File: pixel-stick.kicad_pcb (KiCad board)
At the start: 2 copper layers, 16.5 x 37.1 mm, 16 parts, among them J2 WS28**, U1 AZ1117-3.3, U2 ESP-01v090, U3 SN74LVC1T45DBV, U4 RT9361A

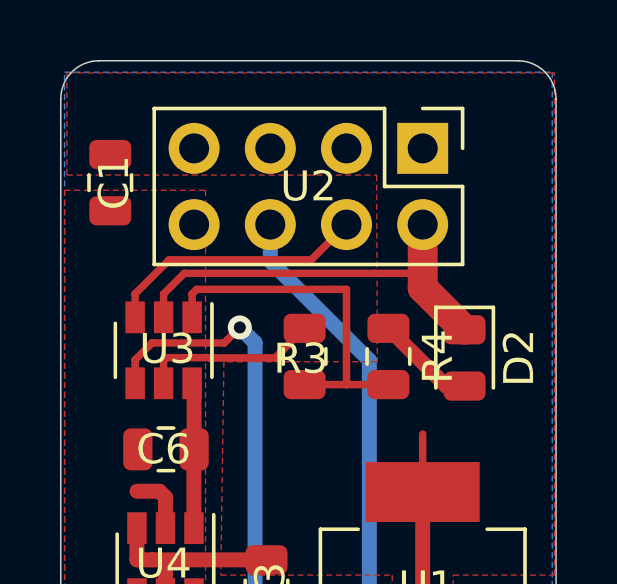
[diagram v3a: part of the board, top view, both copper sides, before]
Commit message: remove programming features
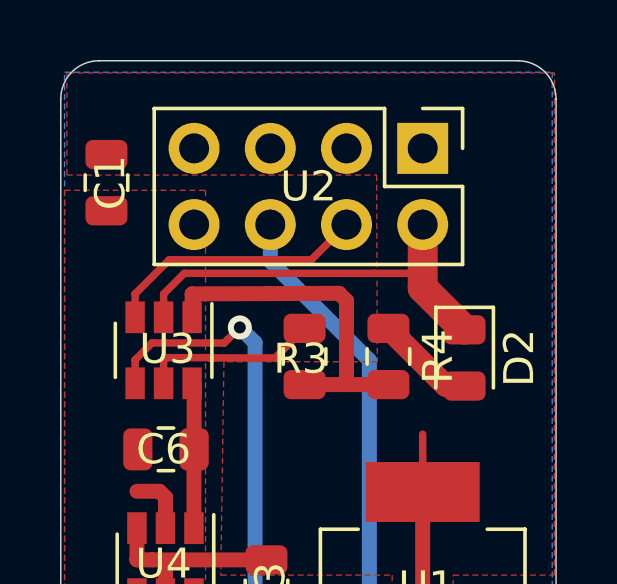
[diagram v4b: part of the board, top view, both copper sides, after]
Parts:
- moved C1 0.13 mm to (44.1, 57.7)
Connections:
- U2 pad 5: /~RST -> +3V3
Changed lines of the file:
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@@
     (thickness 1.6)
     (drawings 13)
-    (tracks 58)
+    (tracks 57)
     (zones 0)
     (modules 16)
-    (nets 17)
+    (nets 16)
   )
   (page A4)
@@
   )
   (setup
-    (last_trace_width 1)
+    (last_trace_width 0.25)
     (user_trace_width 0.5)
     (user_trace_width 1)
@@
   (net 11 /DATA)
   (net 12 /GPIO0)
-  (net 13 /~RST)
-  (net 14 /GPIO2)
-  (net 15 "Net-(R3-Pad1)")
-  (net 16 "Net-(D2-Pad2)")
+  (net 13 /GPIO2)
+  (net 14 "Net-(R3-Pad1)")
+  (net 15 "Net-(D2-Pad2)")
   (net_class Default "This is the default net class."
     (clearance 0.2)
@@
     (add_net /TXD)
     (add_net /VIN)
-    (add_net /~RST)
     (add_net GND)
     (add_net "Net-(C5-Pad1)")
@@
     (fp_line (start 1 -0.6) (end -0.7 -0.6) (layer F.Fab) (width 0.1))
     (pad 2 smd roundrect (at 0.9375 0 270) (size 0.975 1.4) (layers F.Cu F.Paste F.Mask) (roundrect_rratio 0.25)
-      (net 16 "Net-(D2-Pad2)"))
+      (net 15 "Net-(D2-Pad2)"))
     (pad 1 smd roundrect (at -0.9375 0 270) (size 0.975 1.4) (layers F.Cu F.Paste F.Mask) (roundrect_rratio 0.25)
       (net 1 GND))
@@
       (net 2 +3V3))
     (pad 1 smd roundrect (at -0.9375 0 270) (size 0.975 1.4) (layers F.Cu F.Paste F.Mask) (roundrect_rratio 0.25)
-      (net 16 "Net-(D2-Pad2)"))
+      (net 15 "Net-(D2-Pad2)"))
     (model ${KISYS3DMOD}/Resistor_SMD.3dshapes/R_0805_2012Metric.wrl
       (at (xyz 0 0 0))
@@
       (net 12 /GPIO0))
     (pad 5 thru_hole oval (at 0 5.08 270) (size 1.7 1.7) (drill 1) (layers *.Cu *.Mask)
-      (net 13 /~RST))
+      (net 2 +3V3))
     (pad 4 thru_hole oval (at 2.54 2.54 270) (size 1.7 1.7) (drill 1) (layers *.Cu *.Mask)
-      (net 14 /GPIO2))
+      (net 13 /GPIO2))
     (pad 3 thru_hole oval (at 0 2.54 270) (size 1.7 1.7) (drill 1) (layers *.Cu *.Mask)
       (net 2 +3V3))
@@
     )
     (pad 5 smd rect (at 1.1 0 270) (size 1.06 0.65) (layers F.Cu F.Paste F.Mask)
-      (net 15 "Net-(R3-Pad1)"))
+      (net 14 "Net-(R3-Pad1)"))
     (pad 6 smd rect (at 1.1 -0.95 270) (size 1.06 0.65) (layers F.Cu F.Paste F.Mask)
       (net 6 +5V))
@@
       (net 11 /DATA))
     (pad 3 smd rect (at -1.1 0.95 270) (size 1.06 0.65) (layers F.Cu F.Paste F.Mask)
-      (net 14 /GPIO2))
+      (net 13 /GPIO2))
     (pad 2 smd rect (at -1.1 0 270) (size 1.06 0.65) (layers F.Cu F.Paste F.Mask)
       (net 1 GND))
@@
       (net 2 +3V3))
     (pad 1 smd roundrect (at -0.9375 0 270) (size 0.975 1.4) (layers F.Cu F.Paste F.Mask) (roundrect_rratio 0.25)
-      (net 15 "Net-(R3-Pad1)"))
+      (net 14 "Net-(R3-Pad1)"))
     (model ${KISYS3DMOD}/Resistor_SMD.3dshapes/R_0805_2012Metric.wrl
       (at (xyz 0 0 0))
@@
   )
   (module Capacitor_SMD:C_0805_2012Metric (layer F.Cu)
-    (at 44.196 57.658 270)
+    (at 44.069 57.658 270)
     (descr "Capacitor SMD 0805 (2012 Metric), square (rectangular) end terminal, IPC_7351 nominal, (Body size source: https://docs.google.com/spreadsheets/d/1BsfQQcO9C6DZCsRaXUlFlo91Tg2WpOkGARC1WS5S8t0/edit?usp=sharing), generated with kicad-footprint-generator")
     (tags capacitor)
@@
   (segment (start 52.04 56.485) (end 52.07 56.515) (width 0.25) (layer B.Cu) (net 2))
   (segment (start 54.61 74.27) (end 54.61 67.97) (width 0.5) (layer F.Cu) (net 2))
-  (segment (start 46.924 61.366) (end 47.076 61.214) (width 0.25) (layer F.Cu) (net 2))
-  (segment (start 46.924 62.146) (end 46.924 61.366) (width 0.25) (layer F.Cu) (net 2))
   (segment (start 54.61 66.04) (end 54.61 67.97) (width 0.25) (layer F.Cu) (net 2))
   (segment (start 45.085 69.174) (end 45.085 70.231) (width 0.5) (layer F.Cu) (net 2))
@@
   (segment (start 45.593 70.231) (end 49.403 70.231) (width 0.5) (layer F.Cu) (net 2))
   (segment (start 45.085 70.231) (end 45.593 70.231) (width 0.5) (layer F.Cu) (net 2))
-  (segment (start 47.076 61.214) (end 51.532 61.214) (width 0.25) (layer F.Cu) (net 2))
-  (segment (start 52.07 64.389) (end 52.07 61.214) (width 0.25) (layer F.Cu) (net 2))
-  (segment (start 51.532 61.214) (end 52.07 61.214) (width 0.25) (layer F.Cu) (net 2))
-  (segment (start 50.673 64.389) (end 52.07 64.389) (width 0.25) (layer F.Cu) (net 2))
-  (segment (start 52.07 64.389) (end 53.467 64.389) (width 0.25) (layer F.Cu) (net 2))
+  (segment (start 50.673 64.389) (end 52.07 64.389) (width 0.5) (layer F.Cu) (net 2))
+  (segment (start 52.07 64.389) (end 53.467 64.389) (width 0.5) (layer F.Cu) (net 2))
+  (segment (start 46.924 62.146) (end 46.924 61.366) (width 0.5) (layer F.Cu) (net 2))
+  (segment (start 52.07 61.595) (end 51.820716 61.345716) (width 0.5) (layer F.Cu) (net 2))
+  (segment (start 52.07 64.389) (end 52.07 61.595) (width 0.5) (layer F.Cu) (net 2))
+  (segment (start 46.924 61.366) (end 51.820716 61.345716) (width 0.5) (layer F.Cu) (net 2))
   (segment (start 45.115 71.404) (end 45.085 71.374) (width 0.5) (layer F.Cu) (net 4))
   (segment (start 45.115 73.914) (end 45.115 71.404) (width 0.5) (layer F.Cu) (net 4))
@@
   (segment (start 49.53 60.276314) (end 52.832 63.578314) (width 0.5) (layer B.Cu) (net 12))
   (segment (start 49.53 59.055) (end 49.53 60.276314) (width 0.5) (layer B.Cu) (net 12))
-  (segment (start 45.024 61.366) (end 45.024 62.146) (width 0.25) (layer F.Cu) (net 14))
-  (segment (start 46.159999 60.230001) (end 45.024 61.366) (width 0.25) (layer F.Cu) (net 14))
-  (segment (start 50.894999 60.230001) (end 46.159999 60.230001) (width 0.25) (layer F.Cu) (net 14))
-  (segment (start 52.07 59.055) (end 50.894999 60.230001) (width 0.25) (layer F.Cu) (net 14))
-  (segment (start 49.687 63.5) (end 50.673 62.514) (width 0.25) (layer F.Cu) (net 15))
-  (segment (start 46.049001 63.490999) (end 47.509001 63.490999) (width 0.25) (layer F.Cu) (net 15))
-  (segment (start 47.518002 63.5) (end 49.687 63.5) (width 0.25) (layer F.Cu) (net 15))
-  (segment (start 47.509001 63.490999) (end 47.518002 63.5) (width 0.25) (layer F.Cu) (net 15))
-  (segment (start 45.974 63.566) (end 46.049001 63.490999) (width 0.25) (layer F.Cu) (net 15))
-  (segment (start 45.974 64.346) (end 45.974 63.566) (width 0.25) (layer F.Cu) (net 15))
-  (segment (start 55.369 64.389) (end 55.372 64.392) (width 0.25) (layer F.Cu) (net 16))
-  (segment (start 55.3905 64.4375) (end 56.007 64.4375) (width 0.5) (layer F.Cu) (net 16))
-  (segment (start 53.467 62.514) (end 55.3905 64.4375) (width 0.5) (layer F.Cu) (net 16))
+  (segment (start 45.024 61.366) (end 45.024 62.146) (width 0.25) (layer F.Cu) (net 13))
+  (segment (start 50.894999 60.230001) (end 46.159999 60.230001) (width 0.25) (layer F.Cu) (net 13))
+  (segment (start 52.07 59.055) (end 50.894999 60.230001) (width 0.25) (layer F.Cu) (net 13))
+  (segment (start 46.159999 60.230001) (end 45.024 61.366) (width 0.25) (layer F.Cu) (net 13))
+  (segment (start 49.687 63.5) (end 50.673 62.514) (width 0.25) (layer F.Cu) (net 14))
+  (segment (start 46.049001 63.490999) (end 47.509001 63.490999) (width 0.25) (layer F.Cu) (net 14))
+  (segment (start 47.518002 63.5) (end 49.687 63.5) (width 0.25) (layer F.Cu) (net 14))
+  (segment (start 47.509001 63.490999) (end 47.518002 63.5) (width 0.25) (layer F.Cu) (net 14))
+  (segment (start 45.974 63.566) (end 46.049001 63.490999) (width 0.25) (layer F.Cu) (net 14))
+  (segment (start 45.974 64.346) (end 45.974 63.566) (width 0.25) (layer F.Cu) (net 14))
+  (segment (start 55.369 64.389) (end 55.372 64.392) (width 0.25) (layer F.Cu) (net 15))
+  (segment (start 55.3905 64.4375) (end 56.007 64.4375) (width 0.5) (layer F.Cu) (net 15))
+  (segment (start 53.467 62.514) (end 55.3905 64.4375) (width 0.75) (layer F.Cu) (net 15))
   (zone (net 1) (net_name GND) (layer F.Cu) (hatch edge 0.508)
     (connect_pads (clearance 0.508))

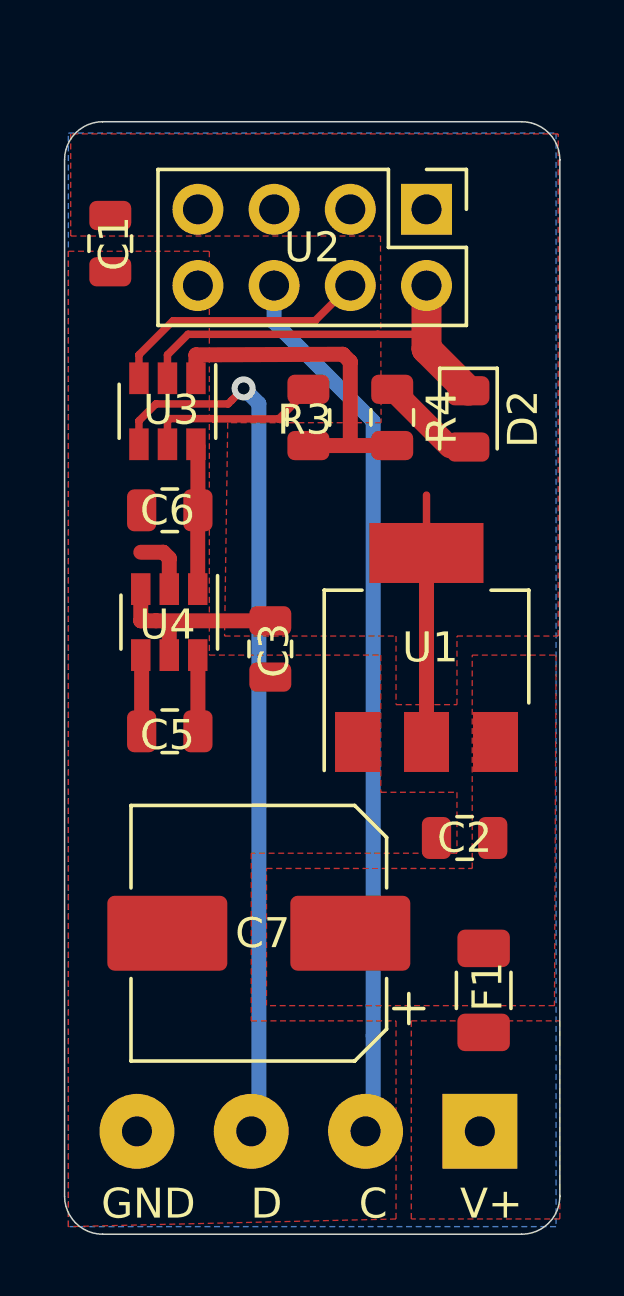
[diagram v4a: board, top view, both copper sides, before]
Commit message: cleanup silkscreen layer
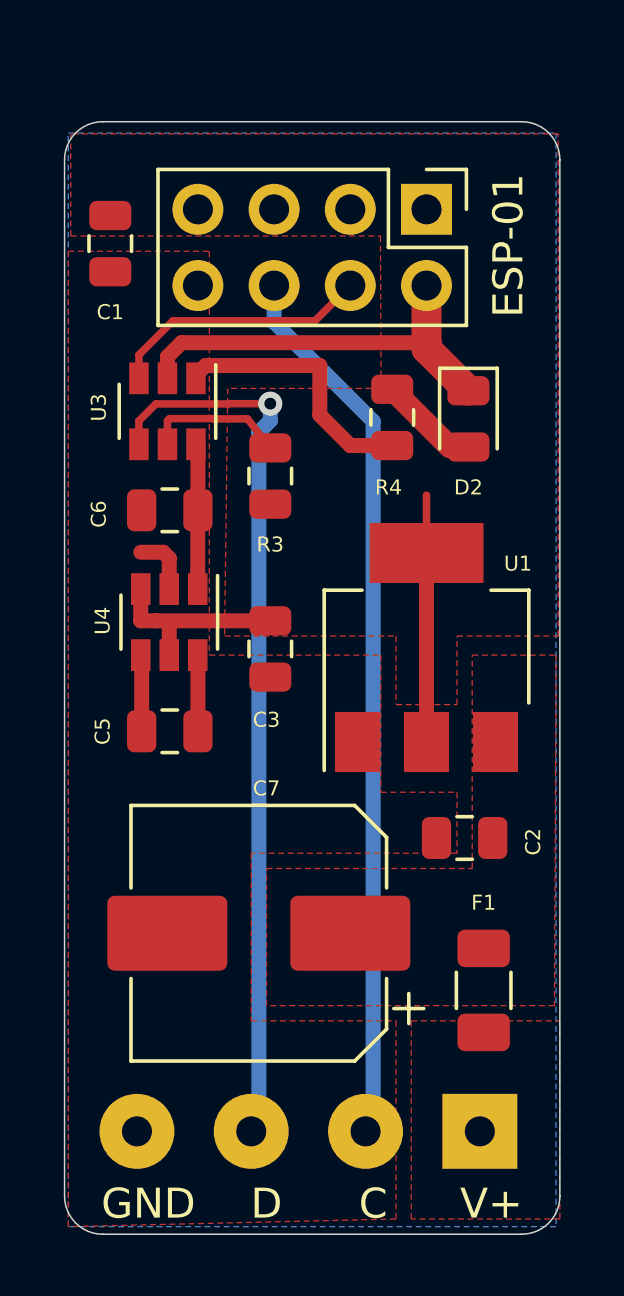
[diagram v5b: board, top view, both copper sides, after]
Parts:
- moved R3 2.33 mm to (49.4, 65.4)
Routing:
- net +3V3: track 26.3 -> 23.6 mm
- net Net-(R3-Pad1): track 5.92 -> 5.09 mm
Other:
- board text added: "ESP-01"

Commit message: update silkscreen
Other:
- board text added: "Board Version: 20191206a"
- board text added: "Designed by Kyle Klaus and Scotty Neally in CA"
- board text added: "This is a modified version of the ESPixelStick hardware design by Shelby Merrick. This board is designed to accept a pre-programmed ESP-01 module with the ESPixelStick firmware and operate 5V or 12V WS28xx pixel strings. The board is powered by the bus voltage of the light string and handles all voltage regulation. A 1A poly fuse is included to reduce the risk of damaging the board but no other p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"
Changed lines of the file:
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@@
   (general
     (thickness 1.6)
-    (drawings 14)
+    (drawings 17)
     (tracks 60)
     (zones 0)
@@
   )
   (setup
-    (last_trace_width 0.5)
+    (last_trace_width 0.25)
     (user_trace_width 0.5)
     (user_trace_width 1)
@@
     )
   )
+  (gr_text "Board Version: 20191206a" (at 54.9275 73.151999 90) (layer B.SilkS)
+    (effects (font (size 0.5 0.5) (thickness 0.125)) (justify mirror))
+  )
+  (gr_text "This is a modified version of the ESPixelStick hardware\ndesign by Shelby Merrick. This board is designed to accept \na pre-programmed ESP-01 module with the ESPixelStick \nfirmware and operate 5V or 12V WS28xx pixel strings. \nThe board is powered by the bus voltage of the light string \nand handles all voltage regulation. A 1A poly fuse is \nincluded to reduce the risk of damaging the board but \nno other protection is included." (at 49.9745 73.151999 90) (layer B.SilkS)
+    (effects (font (size 0.5 0.5) (thickness 0.125)) (justify mirror))
+  )
+  (gr_text "Designed by Kyle Klaus and Scotty Neally in CA" (at 56.769 73.151999 90) (layer B.SilkS)
+    (effects (font (size 0.5 0.5) (thickness 0.125)) (justify mirror))
+  )
   (gr_text ESP-01 (at 57.3405 57.7215 90) (layer F.SilkS)
     (effects (font (size 1 1) (thickness 0.15)))
   )
-  (gr_text "ESPixelStick Mini\n" (at 46.736 71.374 90) (layer B.SilkS)
+  (gr_text "ESPixelStick Mini\n" (at 44.7675 73.152 90) (layer B.SilkS)
     (effects (font (size 1 1) (thickness 0.15)) (justify mirror))
   )
-  (gr_text V+ (at 56.769 89.662) (layer F.SilkS)
+  (gr_text V+ (at 56.5785 89.662) (layer F.SilkS)
     (effects (font (size 1 1) (thickness 0.15)))
   )
-  (gr_text C (at 52.832 89.662) (layer F.SilkS)
+  (gr_text C (at 52.6415 89.662) (layer F.SilkS)
     (effects (font (size 1 1) (thickness 0.15)))
   )
-  (gr_text GND (at 45.339 89.662) (layer F.SilkS)
+  (gr_text GND (at 44.958 89.662) (layer F.SilkS)
     (effects (font (size 1 1) (thickness 0.15)))
   )
-  (gr_text D (at 49.276 89.662) (layer F.SilkS)
+  (gr_text D (at 48.895 89.662) (layer F.SilkS)
     (effects (font (size 1 1) (thickness 0.15)))
   )

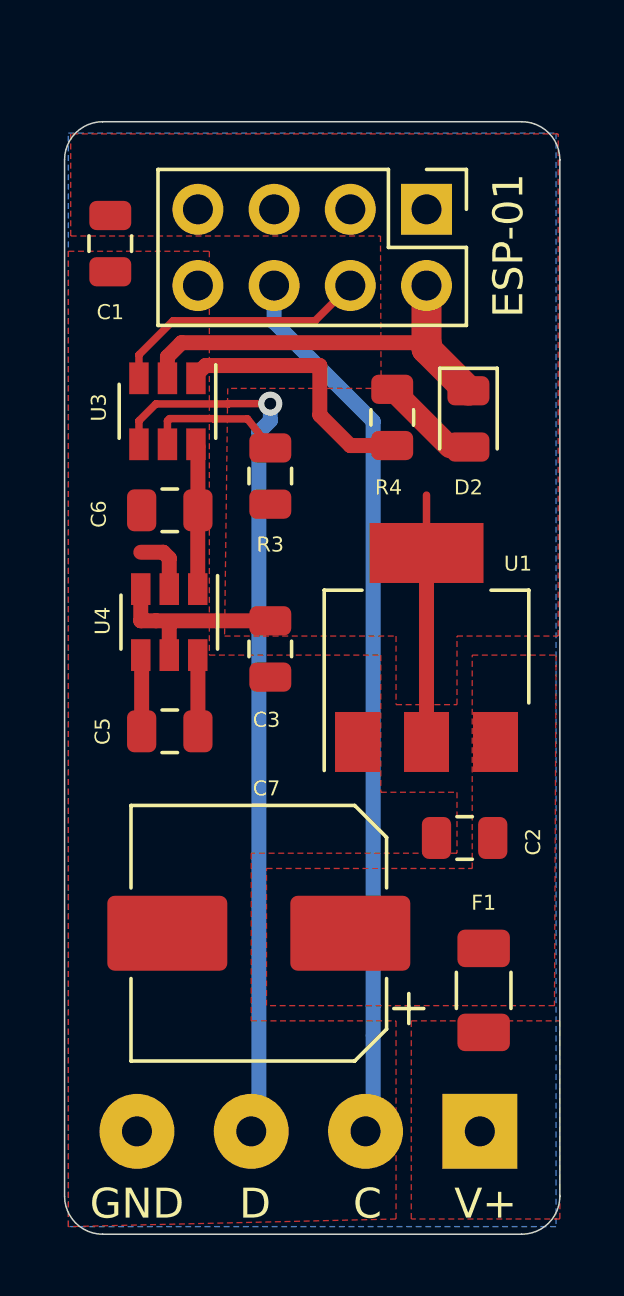
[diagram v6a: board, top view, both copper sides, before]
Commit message: replace logic chip with simple buffer
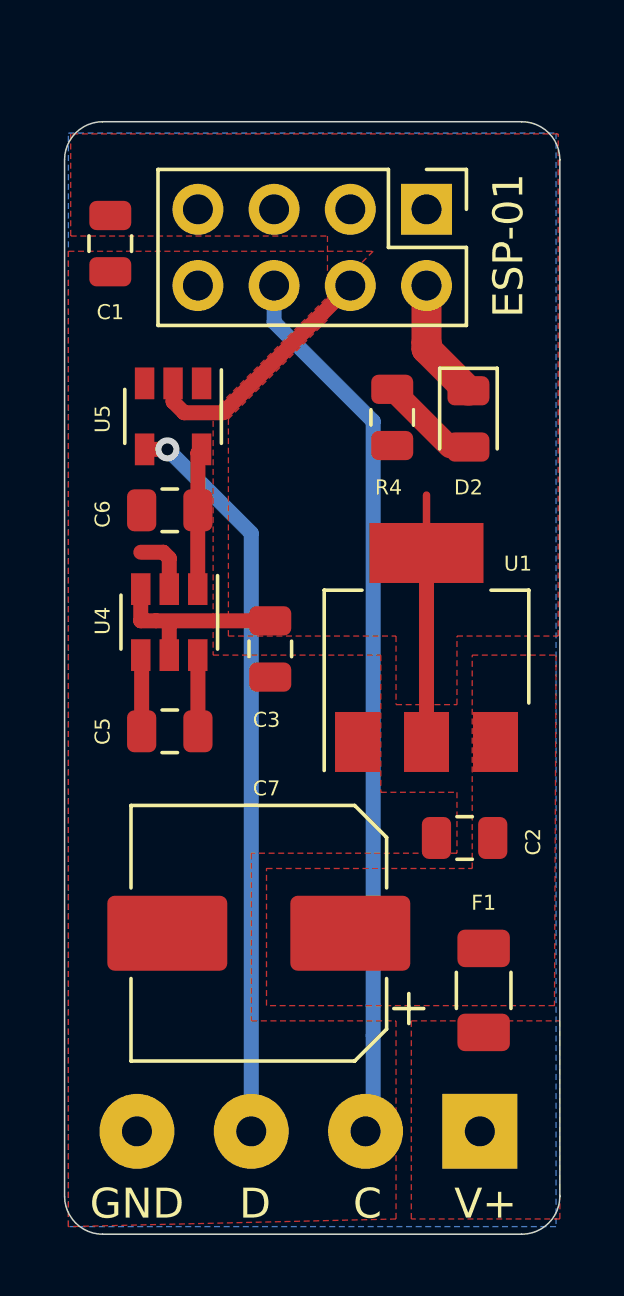
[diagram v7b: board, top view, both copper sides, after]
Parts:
- removed R3: 10k, Resistor_SMD:R_0805_2012Metric
- removed U3: SN74LVC1T45DBV, Package_TO_SOT_SMD:SOT-23-6
- added U5: 74AHC1G125, Package_TO_SOT_SMD:SOT-23-5, F.Cu at (46.2, 63.4)
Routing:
- net GND: track 16.1 -> 6.54 mm
- net +3V3: track 23.6 -> 14.7 mm
- net /DATA: track 29.8 -> 24.7 mm
- net Net-(R3-Pad1): track 5.09 -> 0.00 mm
